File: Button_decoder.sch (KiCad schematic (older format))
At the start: 18 parts, among them U3 74148

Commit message: Aktuell gefertigte Variante
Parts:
- R10, R11, R12: value 120 -> 220
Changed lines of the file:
@@
 P 3700 5500
 F 0 "R10" V 3504 5500 50  0000 C CNN
-F 1 "120" V 3595 5500 50  0000 C CNN
+F 1 "220" V 3595 5500 50  0000 C CNN
 F 2 "Resistor_SMD:R_0603_1608Metric_Pad1.05x0.95mm_HandSolder" H 3700 5500 50  0001 C CNN
 F 3 "~" H 3700 5500 50  0001 C CNN
@@
 P 3700 5800
 F 0 "R11" V 3504 5800 50  0000 C CNN
-F 1 "120" V 3595 5800 50  0000 C CNN
+F 1 "220" V 3595 5800 50  0000 C CNN
 F 2 "Resistor_SMD:R_0603_1608Metric_Pad1.05x0.95mm_HandSolder" H 3700 5800 50  0001 C CNN
 F 3 "~" H 3700 5800 50  0001 C CNN
@@
 P 3700 6100
 F 0 "R12" V 3504 6100 50  0000 C CNN
-F 1 "120" V 3595 6100 50  0000 C CNN
+F 1 "220" V 3595 6100 50  0000 C CNN
 F 2 "Resistor_SMD:R_0603_1608Metric_Pad1.05x0.95mm_HandSolder" H 3700 6100 50  0001 C CNN
 F 3 "~" H 3700 6100 50  0001 C CNN

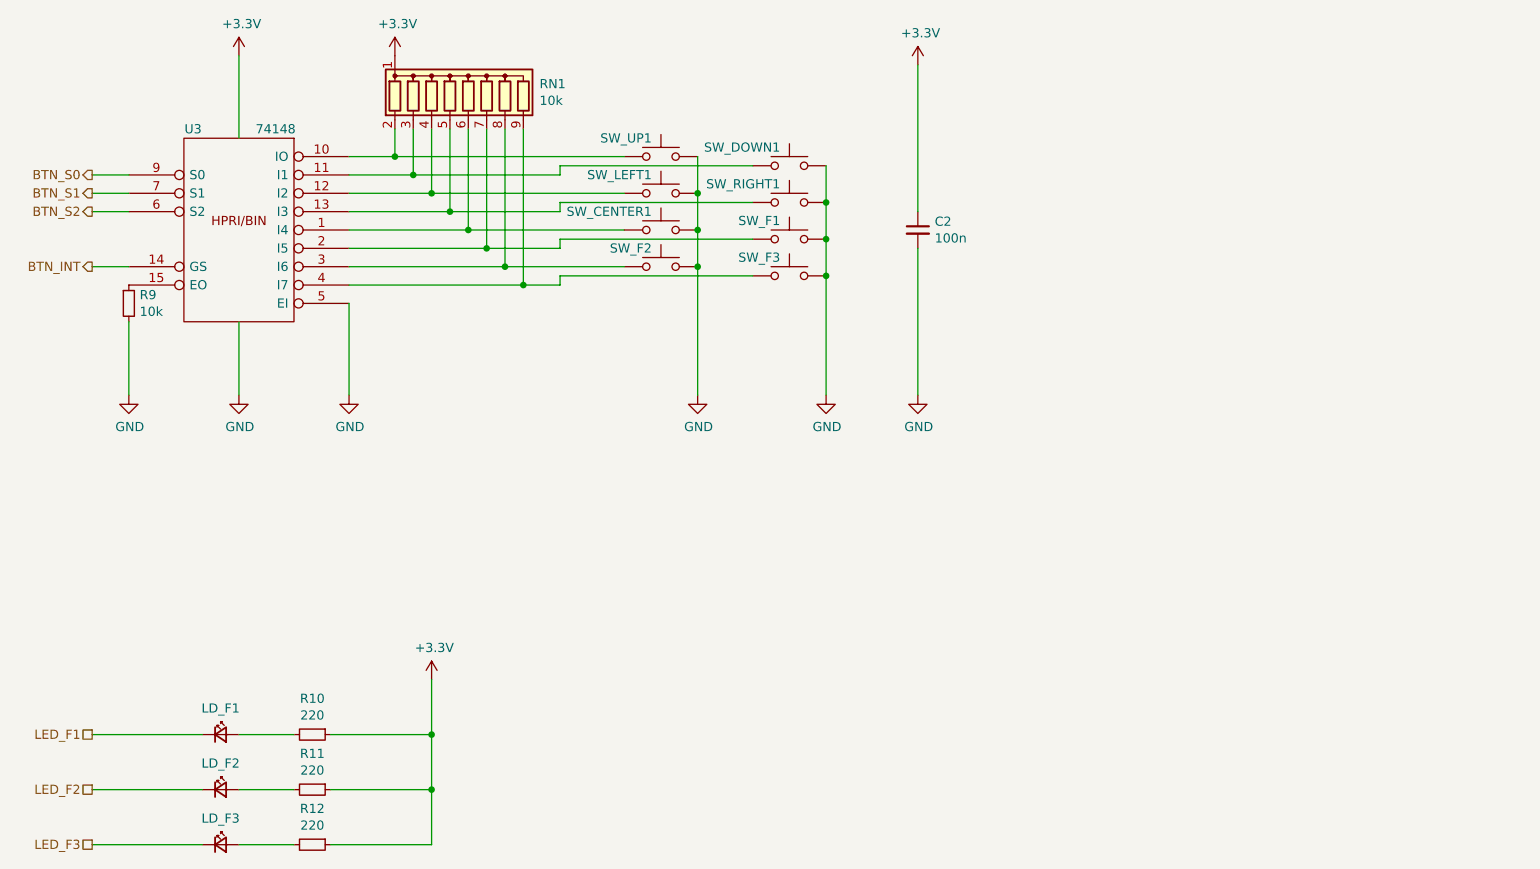
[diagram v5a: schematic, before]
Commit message: Alternative Footprints für Taster und LCD eingefügt
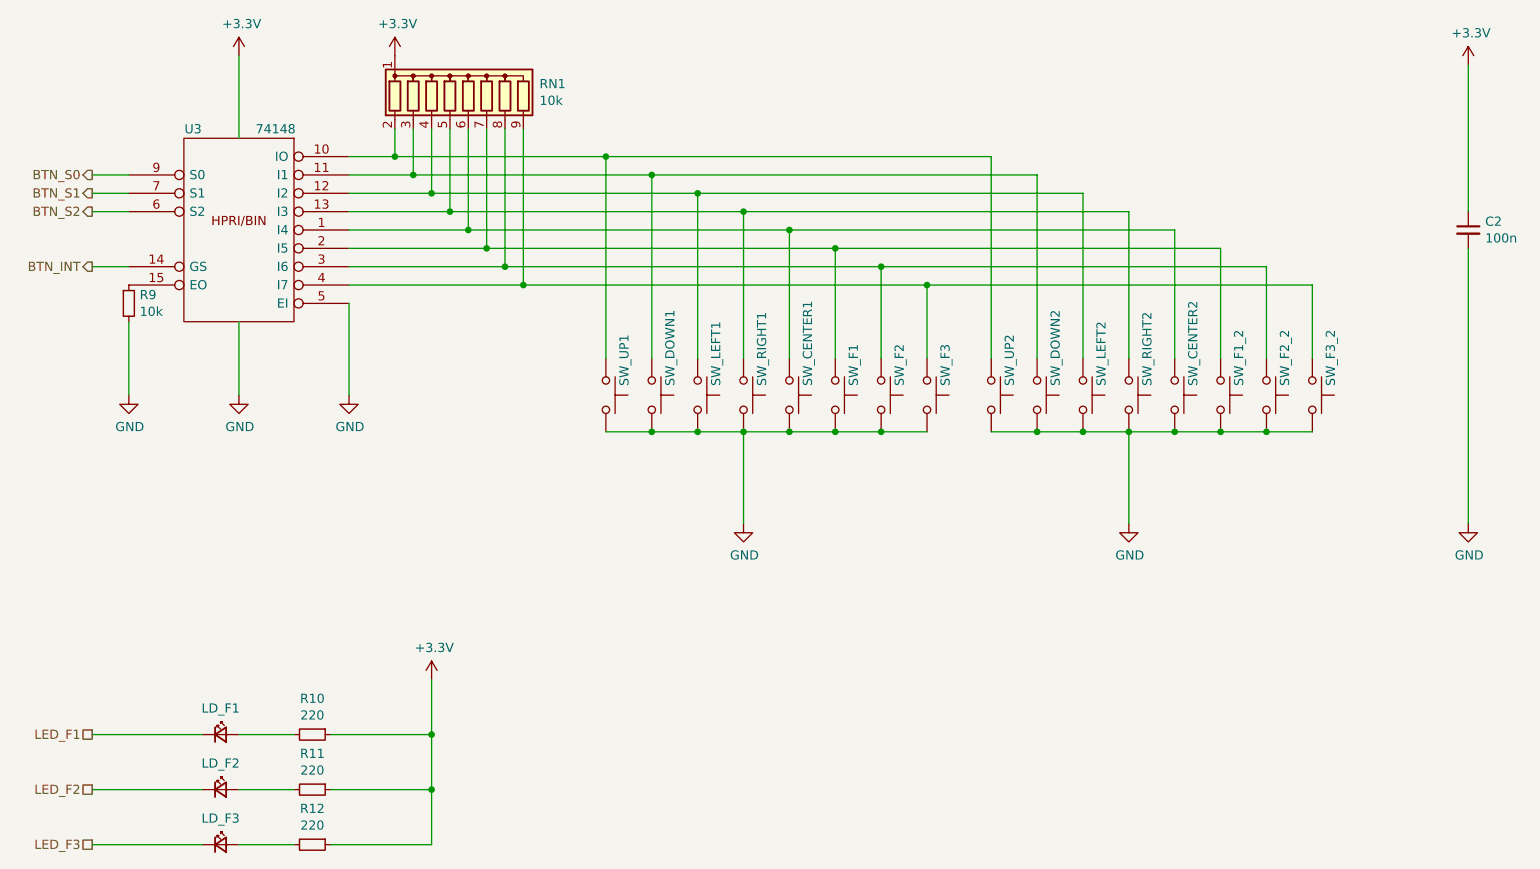
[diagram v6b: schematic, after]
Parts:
- added SW_CENTER2, SW_DOWN2, SW_F2_2, SW_F3_2, SW_LEFT2, SW_RIGHT2, SW_UP2: SW_MEC_5G, Button_Switch_SMD:SW_SPST_Omron_B3FS-100xP, symbol MCT_Labor_5529-rescue:SW_MEC_5G-Switch
- added SW_F1_2: SW_MEC_5, Button_Switch_SMD:SW_SPST_Omron_B3FS-100xP, symbol MCT_Labor_5529-rescue:SW_MEC_5G-Switch
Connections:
- net GND: now also SW_CENTER2.3 (B), SW_CENTER2.4 (B), SW_DOWN2.3 (B), SW_DOWN2.4 (B), SW_F1_2.3 (B), SW_F1_2.4 (B), SW_F2_2.3 (B), SW_F2_2.4 (B), SW_F3_2.3 (B), SW_F3_2.4 (B), SW_LEFT2.3 (B), SW_LEFT2.4 (B), SW_RIGHT2.3 (B), SW_RIGHT2.4 (B), SW_UP2.3 (B), SW_UP2.4 (B)
- net at RN1.6 (R5), SW_CENTER1.1 (A), SW_CENTER1.2 (A)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: now also SW_CENTER2.1 (A), SW_CENTER2.2 (A)
- net at RN1.2 (R1), SW_UP1.1 (A), SW_UP1.2 (A)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: now also SW_UP2.1 (A), SW_UP2.2 (A)
- net at RN1.3 (R2), SW_DOWN1.1 (A), SW_DOWN1.2 (A)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: now also SW_DOWN2.1 (A), SW_DOWN2.2 (A)
- net at RN1.4 (R3), SW_LEFT1.1 (A), SW_LEFT1.2 (A)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: now also SW_LEFT2.1 (A), SW_LEFT2.2 (A)
- net at RN1.5 (R4), SW_RIGHT1.1 (A), SW_RIGHT1.2 (A)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: now also SW_RIGHT2.1 (A), SW_RIGHT2.2 (A)
- net at RN1.7 (R6), SW_F1.1 (A), SW_F1.2 (A)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: now also SW_F1_2.1 (A), SW_F1_2.2 (A)
- net at RN1.8 (R7), SW_F2.1 (A), SW_F2.2 (A)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: now also SW_F2_2.1 (A), SW_F2_2.2 (A)
- net at RN1.9 (R8), SW_F3.1 (A), SW_F3.2 (A)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: now also SW_F3_2.1 (A), SW_F3_2.2 (A)
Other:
- moved on the sheet: C2, SW_CENTER1, SW_DOWN1, SW_F1, SW_F2, SW_F3, SW_LEFT1, SW_RIGHT1, SW_UP1
